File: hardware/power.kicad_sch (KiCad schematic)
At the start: 40 parts, among them J2 +, J3 -, U1 INA186A3, U2 TPS61022, U24 SGM40661, U3 TPS2116, U4 LP5912-3.3, U5 TPS22810

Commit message: Trim BOM to strictly needed parts, fill sourcing fields, fix library datasheets
Owner review 2026-10-11, schematic only (board not resynced).

Removed (17 parts): D1 TVS (clamps above every IC abs max), R2/R3/C5
INA186 input RC, U5 TPS22810 O4 switch with C16/C129/R9/R10/R87/D2
(VHD pad now on +5V_BST, as Matrix HD boards; HD_EN still holds the
analog VTX off via Q28, R11 kept), R67 selector (PA_VCC is +BATT),
TH1/R70 PA NTC and R84 (patched-ELRS only; GPIO37/GPIO4 no-connect),
C92 and C121 (beyond SX1281 / LP5912 datasheet decoupling).

Changed: D4 WS2812 VDD to +5V (3.5 V min); X3 TCXO pin 1 floating per
the YXC sheet; C122/C123/C134 4.7 uF 0402 -> 0201 GRM035R60J475ME15D.

Sourcing: LCSC numbers for 21 MPN lines (SKUBAAE010 has no listing);
every BOM part keeps MPN + Manufacturer for NextPCB.

Library: 16 unused lib symbols pruned; dead or HTML-only datasheet
links replaced with verified PDF URLs (RTC6705, SE5004L, FL2, X1,
EFM8BB51, BC857BM, FTC252012, HCS1206 shunt, Molex 53047).

Net-class patterns and contract entries for the removed nets dropped;
PINMAP ESP32 rows updated (GPIO36 is ADC1_CH0).

Validation: ERC 0 errors / 2 warnings (baseline); check_netlist 7 ok;
sch_integrate --check idempotent; check_conventions unchanged.

Co-Authored-By: Claude Opus 5.5 <noreply@anthropic.com>
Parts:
- removed C129: 100nF, lib:C_0201_0603Metric_L, symbol Device:C
- removed C16: 10nF, lib:C_0201_0603Metric_L, symbol Device:C
- removed C5: 1uF, lib:C_0201_0603Metric_L, symbol Device:C
- removed D1: SMF5.0A, lib:SOD-123FL_L2.7-W1.8-LS3.7-RD_Dense, symbol lib:SMF5.0A
- removed D2: BAS16LD, lib:Nexperia_SOD882D_L, symbol lib:D_BAS16LD
- removed R10: 18k, lib:R_0201_0603Metric_L, symbol Device:R
- removed R2, R3: 1k, lib:R_0201_0603Metric_L, symbol Device:R
- removed R87: 510k, lib:R_0201_0603Metric_L, symbol Device:R
- removed R9: 33k, lib:R_0201_0603Metric_L, symbol Device:R
- removed U5: TPS22810, lib:WSON-6-1EP_2x2mm_P0.65mm_EP1x1.6mm_L, symbol lib:TPS22810DRVR
- FB1: LCSC (none) -> C525479
- R4: LCSC (none) -> C138139
- R5: LCSC (none) -> C295814
- R7: LCSC (none) -> C273316
- U24: LCSC (none) -> C3294703
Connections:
- net SHUNT_SENSE_N_RC is gone; now on net SHUNT_SENSE_N: U1.5 (-IN)
- net SHUNT_SENSE_P_RC is gone; now on net SHUNT_SENSE_P: U1.4 (+IN)

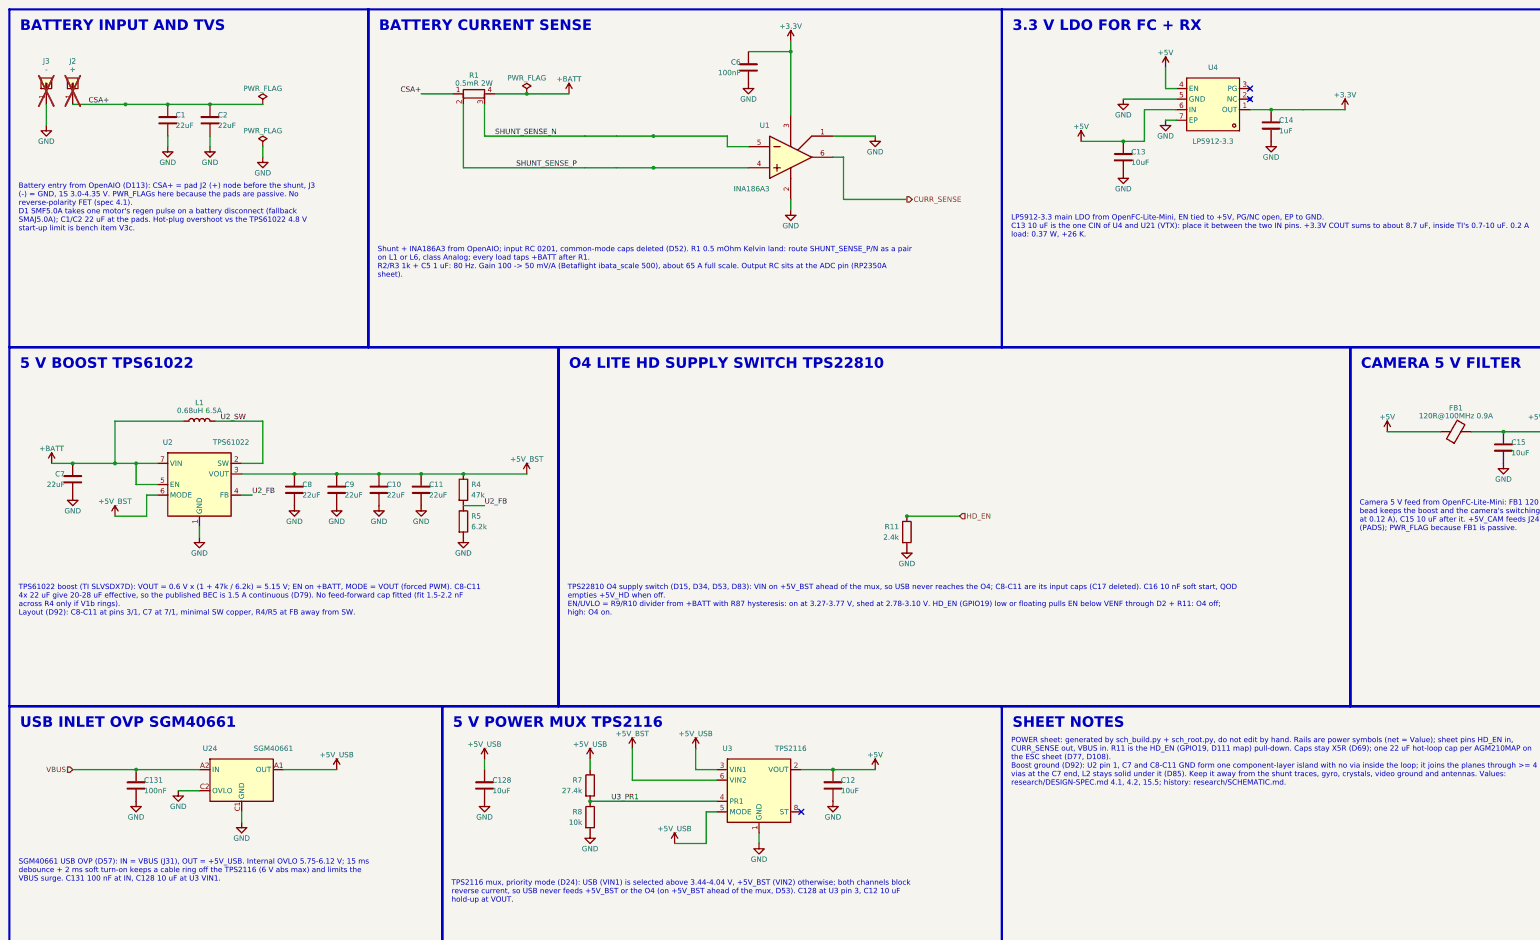
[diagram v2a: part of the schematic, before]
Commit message: 5 V input: two Schottky diodes replace the TPS2116 mux and the SGM40661 (D118)
D9 VBUS -> +5V and D10 +5V_BST -> +5V, MSKSEMI MS2A40LDF DFN1610-2
(LCSC C7380000, imported with import_part.py; land spec PASS). U3, R7,
R8, U24, C131 removed; C128 is +5V bulk; PWR_FLAG on +5V. Board synced.

Stale schematic notes rewritten (O4 switch block now "HD_EN PULL-DOWN",
TVS, INA186 input RC, PA NTC, R67, GPIO4 control, root power table).

ERC 0 errors; check_netlist 7 ok; sch_integrate --check clean;
setup_board --check up to date; board_spec 31/31; sync dry run 0 changes;
DRC unchanged.

Co-Authored-By: Claude Opus 5.5 <noreply@anthropic.com>
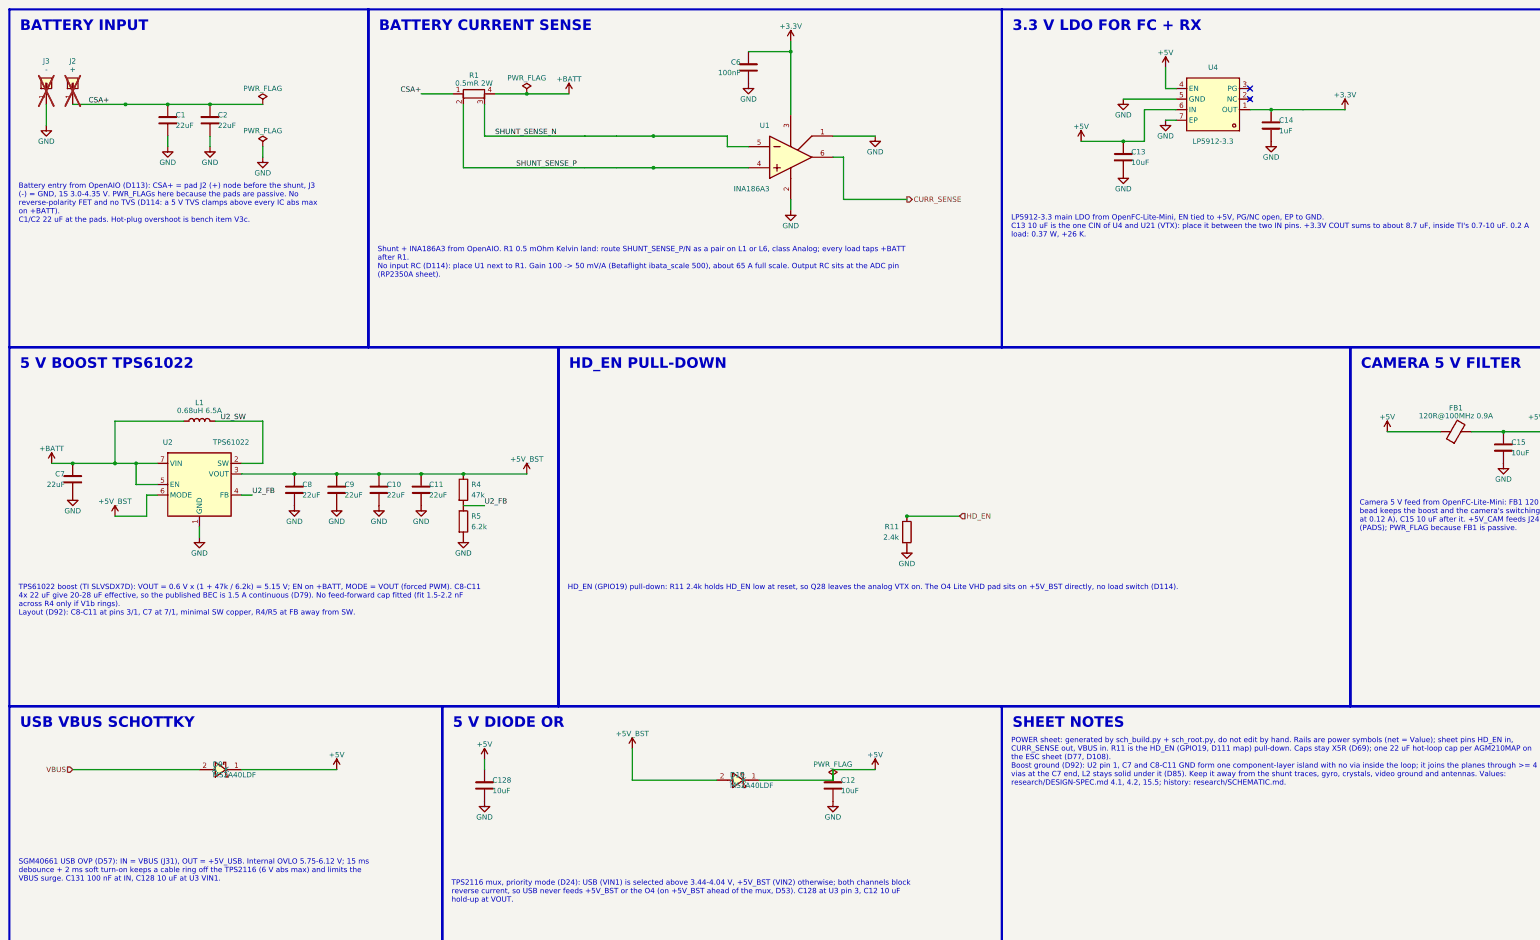
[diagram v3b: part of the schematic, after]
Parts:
- removed C131: 100nF, lib:C_0201_0603Metric_L, symbol Device:C
- removed R7: 27.4k, lib:R_0201_0603Metric_L, symbol Device:R
- removed R8: 10k, lib:R_0201_0603Metric_L, symbol Device:R
- removed U24: SGM40661, lib:WLCSP-6_L1.30-W0.94-P0.40_SGM40661, symbol lib:SGM40661YG
- removed U3: TPS2116, lib:TI_SOT-583_DRL_L, symbol lib:TPS2116DRLR
- added D10, D9: MS2A40LDF, lib:DFN1610-2_L1.6-W1.0-P1.05-RD, symbol lib:MS2A40LDF
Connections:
- net +5V_USB is gone; now on net +5V: C128.1
- net +5V: now also D10.1 (K), D9.1 (K)
- net +5V_BST: now also D10.2 (A)
- net VBUS: now also D9.2 (A)
- no-connect marks 3 -> 2
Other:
- note added: "5 V DIODE OR"
- note added: "BATTERY INPUT"
- note added: "HD_EN PULL-DOWN"
- note added: "USB VBUS SCHOTTKY"
- note removed: "5 V POWER MUX TPS2116"
- note removed: "BATTERY INPUT AND TVS"
- note removed: "O4 LITE HD SUPPLY SWITCH TPS22810"
- note removed: "USB INLET OVP SGM40661"

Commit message: Footprint audit vs datasheets, 0201 lands to Murata minimum, schematic notes shortened
Footprints: 45 checked against their datasheets by group, no pin or
land errors. C/R/L_0201_..._L pad height 0.28 -> 0.30 (Murata GRM03
reflow table c >= 0.30); other lands already at least density per D109
and left unchanged. Land spec texts cleaned (sources, shared parts).

Schematic notes: 157 -> 152 items, 19.5k -> 9.7k characters, all
current (diode-OR, removed parts, RTC6705 filters, TX0/RX0).

check_footprint 107/107 lib specs PASS; ERC 0 errors / 2 warnings;
check_netlist 7 ok; sch_integrate --check clean. Board not synced.

Co-Authored-By: Claude Opus 5.5 <noreply@anthropic.com>
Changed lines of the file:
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@@
 		)
 	)
-	(text_box "Camera 5 V feed from OpenFC-Lite-Mini: FB1 120 Ohm 0.9 A bead keeps the boost and the camera's switching apart (19 mV at 0.12 A), C15 10 uF after it. +5V_CAM feeds J24 and J32 (PADS); PWR_FLAG because FB1 is passive."
+	(text_box "FB1 120 Ohm 0.9 A bead, C15 10 uF after it. +5V_CAM feeds J24 and J32. PWR_FLAG because FB1 is passive."
 		(exclude_from_sim no)
 		(at 339.09 132.08 0)
@@
 		)
 	)
-	(text_box "POWER sheet: generated by sch_build.py + sch_root.py, do not edit by hand. Rails are power symbols (net = Value); sheet pins HD_EN in, CURR_SENSE out, VBUS in. R11 is the HD_EN (GPIO19, D111 map) pull-down. Caps stay X5R (D69); one 22 uF hot-loop cap per AGM210MAP on the ESC sheet (D77, D108).\nBoost ground (D92): U2 pin 1, C7 and C8-C11 GND form one component-layer island with no via inside the loop; it joins the planes through >= 4 vias at the C7 end, L2 stays solid under it (D85). Keep it away from the shunt traces, gyro, crystals, video ground and antennas. Values: research/DESIGN-SPEC.md 4.1, 4.2, 15.5; history: research/SCHEMATIC.md."
+	(text_box "Boost ground: U2 pin 1, C7 and C8-C11 GND form one island with no via inside the loop, joined to the planes by >= 4 vias at C7; keep the L2 plane solid below.\nKeep it away from shunt, gyro, crystals, video, antennas."
 		(exclude_from_sim no)
 		(at 255.27 189.23 0)
@@
 		)
 	)
-	(text_box "Battery entry from OpenAIO (D113): CSA+ = pad J2 (+) node before the shunt, J3 (-) = GND, 1S 3.0-4.35 V. PWR_FLAGs here because the pads are passive. No reverse-polarity FET and no TVS (D114: a 5 V TVS clamps above every IC abs max on +BATT).\nC1/C2 22 uF at the pads. Hot-plug overshoot is bench item V3c."
+	(text_box "CSA+ = J2 (+) node before the shunt, J3 (-) = GND, 1S 3.0-4.35 V. PWR_FLAGs because the pads are passive. No reverse FET, no TVS.\nC1/C2 22 uF at the pads."
 		(exclude_from_sim no)
 		(at 16.51 55.88 0)
@@
 		)
 	)
-	(text_box "TPS2116 mux, priority mode (D24): USB (VIN1) is selected above 3.44-4.04 V, +5V_BST (VIN2) otherwise; both channels block reverse current, so USB never feeds +5V_BST or the O4 (on +5V_BST ahead of the mux, D53). C128 at U3 pin 3, C12 10 uF hold-up at VOUT."
+	(text_box "5 V diode OR: D9 (VBUS) and D10 (+5V_BST) Schottky to +5V, the higher source wins. C12 10 uF at +5V."
 		(exclude_from_sim no)
 		(at 120.65 223.52 0)
@@
 		)
 	)
-	(text_box "TPS61022 boost (TI SLVSDX7D): VOUT = 0.6 V x (1 + 47k / 6.2k) = 5.15 V; EN on +BATT, MODE = VOUT (forced PWM). C8-C11 4x 22 uF give 20-28 uF effective, so the published BEC is 1.5 A continuous (D79). No feed-forward cap fitted (fit 1.5-2.2 nF across R4 only if V1b rings).\nLayout (D92): C8-C11 at pins 3/1, C7 at 7/1, minimal SW copper, R4/R5 at FB away from SW."
+	(text_box "TPS61022: VOUT = 0.6 V x (1 + 47k / 6.2k) = 5.15 V, EN on +BATT, forced PWM, 4x 22 uF (C8-C11), 1.5 A continuous.\nC8-C11 at pins 3/1, C7 at 7/1, minimal SW copper, R4/R5 at FB away from SW."
 		(exclude_from_sim no)
 		(at 16.51 152.4 0)
@@
 		)
 	)
-	(text_box "Shunt + INA186A3 from OpenAIO. R1 0.5 mOhm Kelvin land: route SHUNT_SENSE_P/N as a pair on L1 or L6, class Analog; every load taps +BATT after R1.\nNo input RC (D114): place U1 next to R1. Gain 100 -> 50 mV/A (Betaflight ibata_scale 500), about 65 A full scale. Output RC sits at the ADC pin (RP2350A sheet)."
+	(text_box "R1 0.5 mOhm Kelvin land: route SHUNT_SENSE_P/N as a pair on L1 or L6 (Analog class); every load taps +BATT after R1.\nINA186A3 gain 100 = 50 mV/A: place U1 next to R1."
 		(exclude_from_sim no)
 		(at 102.87 71.12 0)
@@
 		)
 	)
-	(text_box "LP5912-3.3 main LDO from OpenFC-Lite-Mini, EN tied to +5V, PG/NC open, EP to GND.\nC13 10 uF is the one CIN of U4 and U21 (VTX): place it between the two IN pins. +3.3V COUT sums to about 8.7 uF, inside TI's 0.7-10 uF. 0.2 A load: 0.37 W, +26 K."
+	(text_box "LP5912-3.3 U4: EN on +5V, EP to GND. C13 10 uF is the shared CIN of U4 and U21: place it between the two IN pins."
 		(exclude_from_sim no)
 		(at 255.27 63.5 0)
@@
 		)
 	)
-	(text_box "SGM40661 USB OVP (D57): IN = VBUS (J31), OUT = +5V_USB. Internal OVLO 5.75-6.12 V; 15 ms debounce + 2 ms soft turn-on keeps a cable ring off the TPS2116 (6 V abs max) and limits the VBUS surge. C131 100 nF at IN, C128 10 uF at U3 VIN1."
-		(exclude_from_sim no)
-		(at 16.51 218.44 0)
-		(size 101.6 10.16)
-		(margins 0.9525 0.9525 0.9525 0.9525)
-		(stroke
-			(width -0.0001)
-			(type solid)
-		)
-		(fill
-			(type none)
-		)
-		(effects
-			(font
-				(size 1.27 1.27)
-			)
-			(justify left top)
-		)
-	)
-	(text_box "HD_EN (GPIO19) pull-down: R11 2.4k holds HD_EN low at reset, so Q28 leaves the analog VTX on. The O4 Lite VHD pad sits on +5V_BST directly, no load switch (D114)."
+	(text_box "R11 2.4k pulls HD_EN (GPIO19) low at reset: Q28 leaves the analog VTX on. The O4 VHD pad sits on +5V_BST, no load switch."
 		(exclude_from_sim no)
 		(at 148.59 152.4 0)

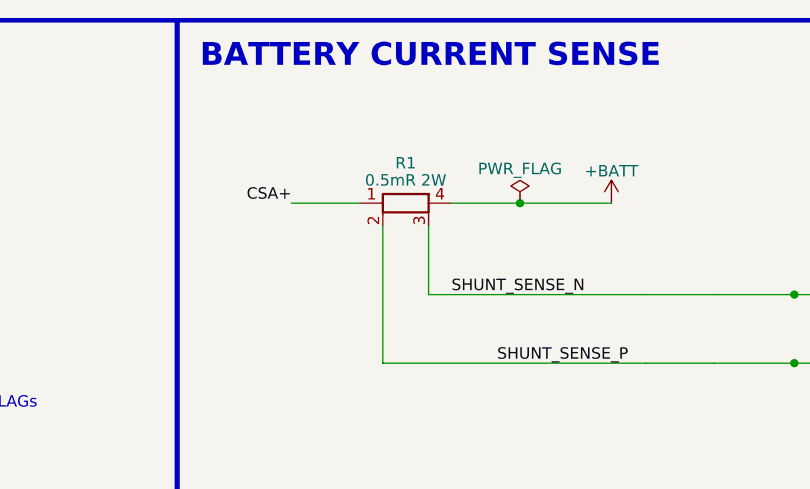
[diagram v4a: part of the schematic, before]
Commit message: Larger solder pads and ESC programming pads, R1 shunt flipped (D120)
All hand-solder pads J20-J29/J33 on SolderPad_1.0x1.2mm; ESC C2 test
pads TP1-TP8 on TestPoint_Pad_D0.8mm; R1 rotated 270 without mirror
(owner edit, Kelvin pairs and INA186 polarity unchanged). ERC 0 errors;
check_netlist 7 ok.

Co-Authored-By: Claude Opus 5.5 <noreply@anthropic.com>
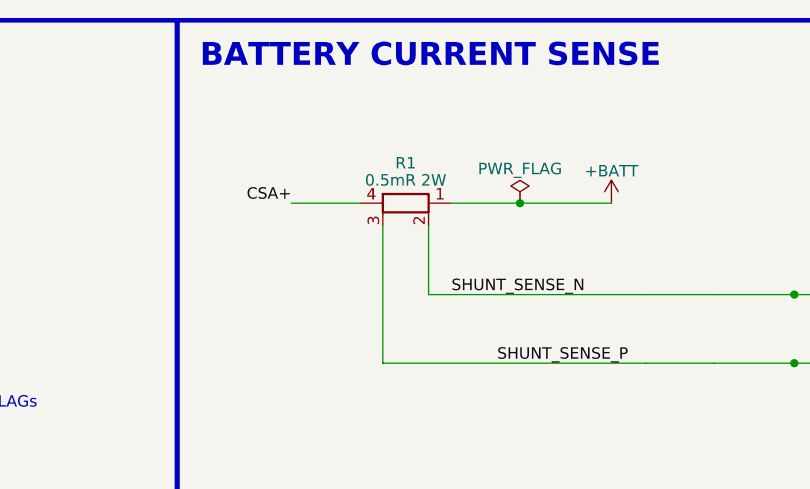
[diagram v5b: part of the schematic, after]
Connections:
- net +BATT: now also R1.1; no longer R1.4
- net CSA+: now also R1.4; no longer R1.1
- net SHUNT_SENSE_N: now also R1.2; no longer R1.3
- net SHUNT_SENSE_P: now also R1.3; no longer R1.2
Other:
- moved on the sheet: R1
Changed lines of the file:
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@@
 	(symbol
 		(lib_id "lib:R_Shunt_Kelvin")
-		(at 127 35.56 90)
-		(mirror x)
+		(at 127 35.56 270)
 		(unit 1)
 		(body_style 1)

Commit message: WIP placement and schematic snapshot for shared routing
Owner placement and schematic edits, firmware bindings, routing notes and
board tooling, so others can try the routing. Not DRC-clean; PCB not yet
updated from the schematic (R1 to R2, C1/C2/C134 removal).

Co-Authored-By: Claude Opus 5.5 <noreply@anthropic.com>
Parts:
- removed C1, C2: 22uF, lib:C_0603_1608Metric_L, symbol Device:C
- removed C13: 10uF, lib:C_0402_1005Metric_L, symbol Device:C
- removed R1: 0.5mR 2W, lib:R_1206_Kelvin_4Pad_NetTie_HCS1206_L, symbol lib:R_Shunt_Kelvin
- removed R11: 2.4k, lib:R_0201_0603Metric_L, symbol Device:R
- added D11: MS2A40LDF, lib:DFN1610-2_L1.6-W1.0-P1.05-RD, symbol lib:MS2A40LDF
- added R2: 0.5mR 2W, lib:R_1206_Kelvin_4Pad_NetTie_HCS1206_L, symbol lib:R_Shunt_Kelvin
- C14: value 1uF -> 4.7uF; LCSC C76935 -> C335103; MPN GRM033R61A105ME44D -> GRM035R60J475ME15D
- U4: value LP5912-3.3 -> TLV75733; symbol lib:LP5912-3.3DRVR -> lib:TLV75733PDRVR; LCSC C524780 -> C2868428; MPN LP5912-3.3DRVR -> TLV75733PDRVR
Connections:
- net +3.3V: now also D11.2 (A)
- net +5V: now also D11.1 (K)
- net +BATT: now also R2.4
- net CSA+: now also R2.1
- net GND: now also U4.3 (GND); no longer U4.5 (GND)
- net SHUNT_SENSE_N: now also R2.3
- net SHUNT_SENSE_P: now also R2.2
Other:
- note added: "LDO REVERSE-CURRENT BYPASS"
- note removed: "HD_EN PULL-DOWN"

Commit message: fix(schematic-review): BEMF check N7, review docs, D125 (#14)
* docs+check: BEMF phase-sense rule N7, review docs (limits, VTX path, Wi-Fi network absent, D125)

Schematic edits (BEMF swap, U4 text box, J2 note) are listed as manual Eeschema
steps in the PR: kicad-skip 0.2.5 does not round-trip these KiCad 10 files.

Co-Authored-By: Claude Opus 5.5 <noreply@anthropic.com>

* docs(readme): limits and VTX path tables under Constraints (keeps check_conventions D2 at base)

Co-Authored-By: Claude Opus 5.5 <noreply@anthropic.com>

* fix(sch): swap BEMF_B/BEMF_C labels in esc_channel (all four ESCs); correct U4 text box; 1S note at J2

Structured s-expression edit (sexpdata), re-saved by kicad-cli sch upgrade --force;
diff against the baseline re-save contains only the intended changes.

Co-Authored-By: Claude Opus 5.5 <noreply@anthropic.com>

---------

Co-authored-by: Claude Opus 5.5 <noreply@anthropic.com>
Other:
- note added: "1S only, max 4.35 V"
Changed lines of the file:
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@@
+		)
+	)
+	(text "1S only, max 4.35 V"
+		(exclude_from_sim no)
+		(at 38.1 33.02 0)
+		(effects
+			(font
+				(size 1.27 1.27)
+			)
+			(justify left)
 		)
 	)
@@
 		)
 	)
-	(text_box "TLV75733 U4: EN on +5V; GND pin 3 and EP pin 7 grounded; NC pins 2/5. C13 10 uF input, C14 4.7 uF local output.\nU4 permits 1-200 uF COUT; D11 bypasses reverse current during input collapse. Keep the bypass loop short."
+	(text_box "TLV75733 U4: EN on +5V; GND pin 3 and EP pin 7 grounded; pins 2 and 5 not connected. C12 and C128 are the +5V input capacitors, C14 4.7 uF local output.\nU4 permits 1-200 uF COUT; D11 bypasses reverse current during input collapse. Keep the bypass loop short."
 		(exclude_from_sim no)
 		(at 255.27 63.5 0)
